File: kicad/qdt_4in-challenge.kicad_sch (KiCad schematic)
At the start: 44 parts, among them J1 Bus_PCI_Express_x1, J2 Conn_01x02, J3 MSD-4-A, J6 USB_C_Receptacle_USB2.0_16P, U2 RP2040, U4 W25Q128JVP, U9 MCP25625T-E/ML, X1 ABM8-272-T3, Y1 X322516MLB4SI

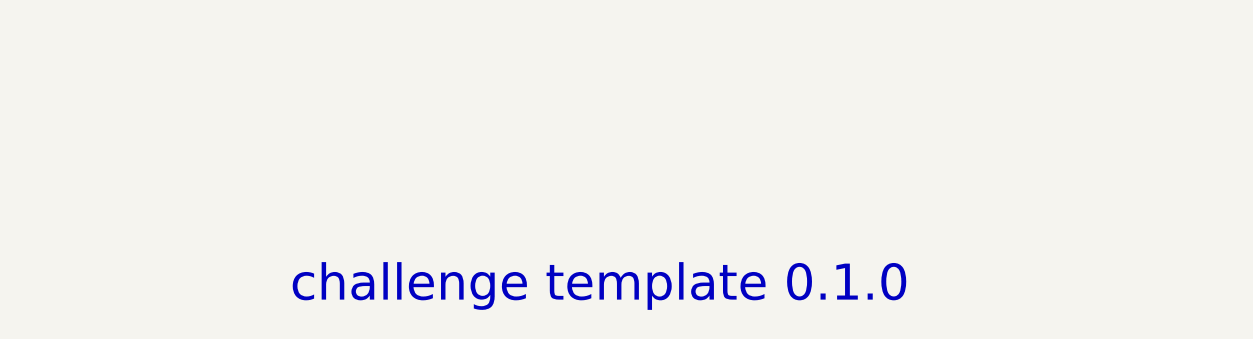
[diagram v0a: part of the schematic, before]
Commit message: Update file names and titles
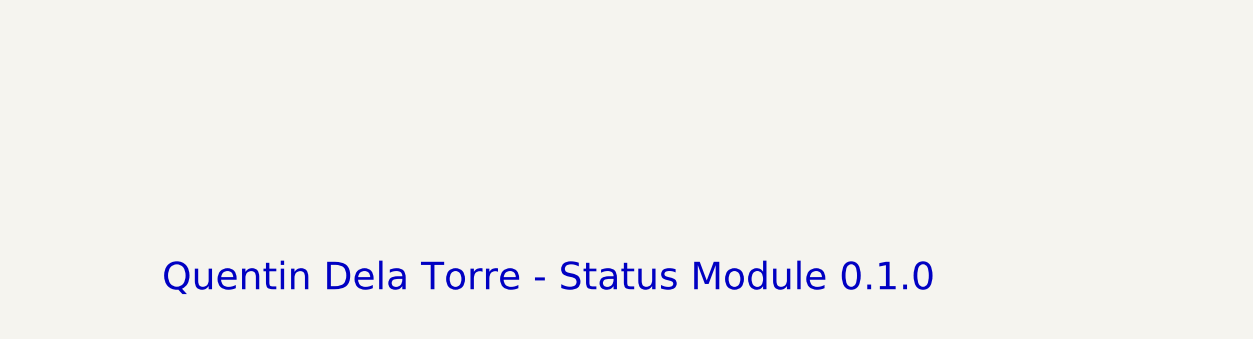
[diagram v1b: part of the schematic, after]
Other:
- note added: "Quentin Dela Torre - Status Module 0.1.0"
- note removed: "challenge template 0.1.0"
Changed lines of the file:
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@@
 		)
 	)
-	(text "challenge template 0.1.0"
+	(text "Quentin Dela Torre - Status Module 0.1.0"
 		(exclude_from_sim no)
-		(at 493.014 386.842 0)
+		(at 478.79 385.572 0)
 		(effects
 			(font
-				(size 4 4)
+				(size 3.048 3.048)
 			)
 			(justify left bottom)

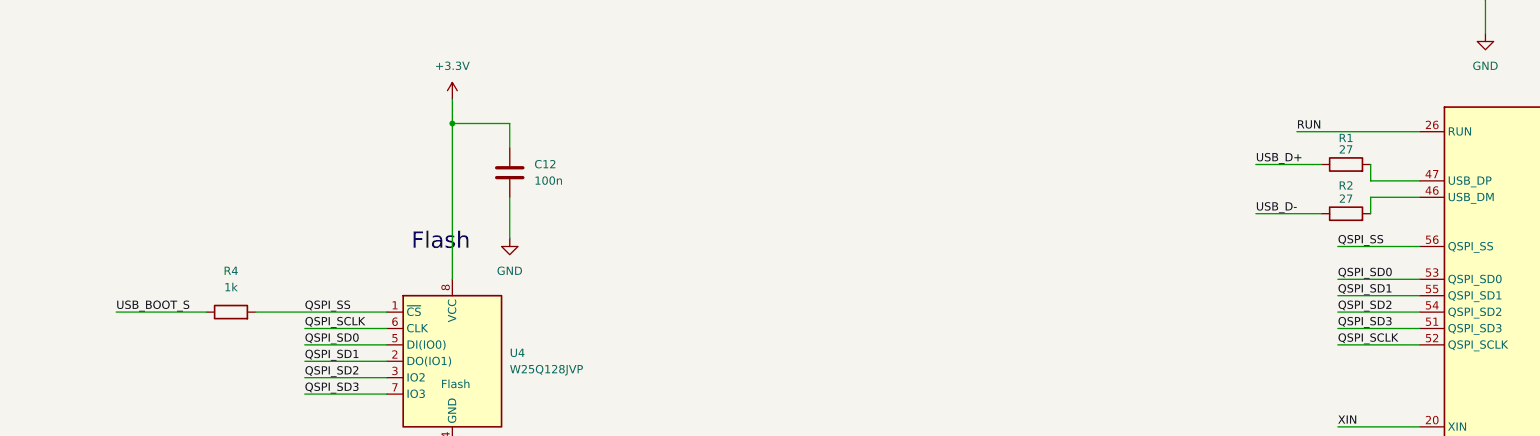
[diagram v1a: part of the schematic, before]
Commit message: Moved components and removed buttons from pcb
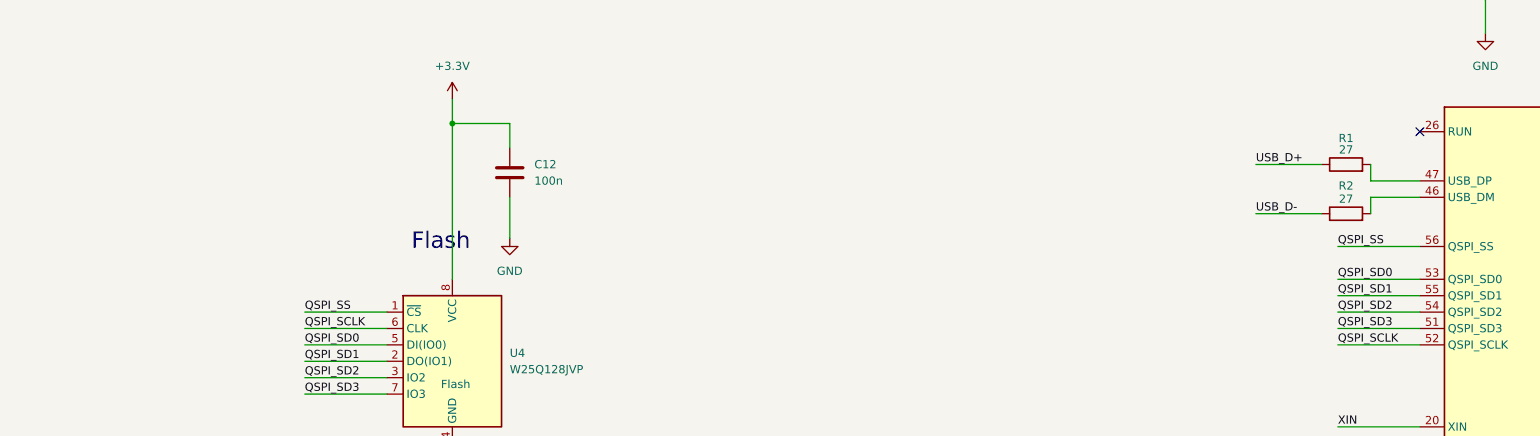
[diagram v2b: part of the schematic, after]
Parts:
- removed R4: 1k, Resistor_SMD:R_0603_1608Metric, symbol Device:R
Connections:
- net RUN: no longer names the net of U2.26 (RUN)
- no-connect marks 36 -> 37
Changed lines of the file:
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@@
 	)
 	(no_connect
+		(at 275.59 140.97)
+	)
+	(no_connect
 		(at 326.39 214.63)
 	)
@@
 	(wire
 		(pts
-			(xy 256.54 140.97) (xy 275.59 140.97)
-		)
-		(stroke
-			(width 0)
-			(type default)
-		)
-	)
-	(wire
-		(pts
 			(xy 364.49 250.19) (xy 367.03 250.19)
 		)
@@
 	(wire
 		(pts
-			(xy 73.66 168.91) (xy 87.63 168.91)
-		)
-		(stroke
-			(width 0)
-			(type default)
-		)
-	)
-	(wire
-		(pts
 			(xy 285.75 120.65) (xy 285.75 125.73)
 		)
@@
 	(wire
 		(pts
-			(xy 95.25 168.91) (xy 115.57 168.91)
+			(xy 102.87 168.91) (xy 115.57 168.91)
 		)
 		(stroke
@@
 		)
 	)
-	(label "RUN"
-		(at 256.54 140.97 0)
-		(effects
-			(font
-				(size 1.27 1.27)
-			)
-			(justify left bottom)
-		)
-	)
-	(label "USB_BOOT_S"
-		(at 73.66 168.91 0)
-		(effects
-			(font
-				(size 1.27 1.27)
-			)
-			(justify left bottom)
-		)
-	)
 	(label "QSPI_SS"
 		(at 262.89 158.75 0)
@@
 					(unit 1)
 				)
-			)
-		)
-	)
-	(symbol
-		(lib_id "Device:R")
-		(at 91.44 168.91 90)
-		(unit 1)
-		(exclude_from_sim no)
-		(in_bom yes)
-		(on_board yes)
-		(dnp no)
-		(fields_autoplaced yes)
-		(property "Reference" "R4"
-			(at 91.44 162.56 90)
-			(effects
-				(font
-					(size 1.27 1.27)
-				)
-			)
-		)
-		(property "Value" "1k"
-			(at 91.44 165.1 90)
-			(effects
-				(font
-					(size 1.27 1.27)
-				)
-			)
-		)
-		(property "Footprint" "Resistor_SMD:R_0603_1608Metric"
-			(at 91.44 170.688 90)
-			(effects
-				(font
-					(size 1.27 1.27)
-				)
-				(hide yes)
-			)
-		)
-		(property "Datasheet" "~"
-			(at 91.44 168.91 0)
-			(effects
-				(font
-					(size 1.27 1.27)
-				)
-				(hide yes)
-			)
-		)
-		(property "Description" "Resistor"
-			(at 91.44 168.91 0)
-			(effects
-				(font
-					(size 1.27 1.27)
-				)
-				(hide yes)
-			)
-		)
-		(pin "1"
-		)
-		(pin "2"
-		)
-		(instances
-			(project ""
-				(path "/612ece3f-e722-4b33-8111-645d24cfcf05"
-					(reference "R4")
-					(unit 1)
-				)
